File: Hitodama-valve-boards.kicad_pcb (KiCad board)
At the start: 2 copper layers, 74.9 x 73.7 mm, 25 parts, among them J1 Solenoid A, J2 Solenoid B, U1 LM358, U2 Pressure_b, U3 Pressure_a, U4 ChamberBoard_Holder, U5 Pololu-713

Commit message: remove useless texts
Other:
- board text removed: "If 1 layer Route only at the back!"
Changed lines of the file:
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@@
   (general
     (thickness 1.6)
-    (drawings 5)
+    (drawings 4)
     (tracks 281)
     (zones 0)
@@
       (effects (font (size 1 1) (thickness 0.15)))
     )
-    (fp_text value "Solenoid B" (at 2.78 7.75 180) (layer F.Fab)
+    (fp_text value "Solenoid B" (at -4.63 1.12 270) (layer F.Fab)
       (effects (font (size 1 1) (thickness 0.15)))
     )
@@
     (tags "mounting hole 3.2mm no annular m3")
     (attr virtual)
-    (fp_text reference H1 (at 0 -4.2) (layer F.SilkS)
+    (fp_text reference H1 (at 0 -4.2) (layer F.SilkS) hide
       (effects (font (size 1 1) (thickness 0.15)))
     )
@@
     (tags "mounting hole 3.2mm no annular m3")
     (attr virtual)
-    (fp_text reference H2 (at 0 4.2) (layer B.SilkS)
+    (fp_text reference H2 (at -0.5 5.25) (layer B.SilkS) hide
       (effects (font (size 1 1) (thickness 0.15)) (justify mirror))
     )
-    (fp_text value MountingHole (at 0 -4.2) (layer B.Fab)
+    (fp_text value MountingHole (at 0 -4.2) (layer B.Fab) hide
       (effects (font (size 1 1) (thickness 0.15)) (justify mirror))
     )
@@
       (effects (font (size 1 1) (thickness 0.15)) (justify mirror))
     )
-    (fp_text value MountingHole (at 0 6.54) (layer B.Fab)
+    (fp_text value MountingHole (at 0 6.54) (layer B.Fab) hide
       (effects (font (size 1 1) (thickness 0.15)) (justify mirror))
     )
@@
       (effects (font (size 1 1) (thickness 0.15)) (justify mirror))
     )
-    (fp_text value MountingHole (at 0 -4.2) (layer B.Fab)
+    (fp_text value MountingHole (at 0.1 -6.3441) (layer B.Fab) hide
       (effects (font (size 1 1) (thickness 0.15)) (justify mirror))
     )
@@
       (effects (font (size 1 1) (thickness 0.15)))
     )
-    (fp_text value "Solenoid A" (at 2.78 7.75 180) (layer F.Fab)
+    (fp_text value "Solenoid A" (at -4.75 1.07 270) (layer F.Fab)
       (effects (font (size 1 1) (thickness 0.15)))
     )
@@
     )
   )
-  (gr_text "If 1 layer Route only at the back!" (at 19 -4) (layer F.Cu)
-    (effects (font (size 1.5 1.5) (thickness 0.3)))
-  )
   (gr_line (start 74.93 73.66) (end 74.93 0) (layer Edge.Cuts) (width 0.15))

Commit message: generate seedstudio gerber files
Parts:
- added G***: LOGO, Hitodama_Logo:hitodama_n, F.Cu at (53.4, 67.2)

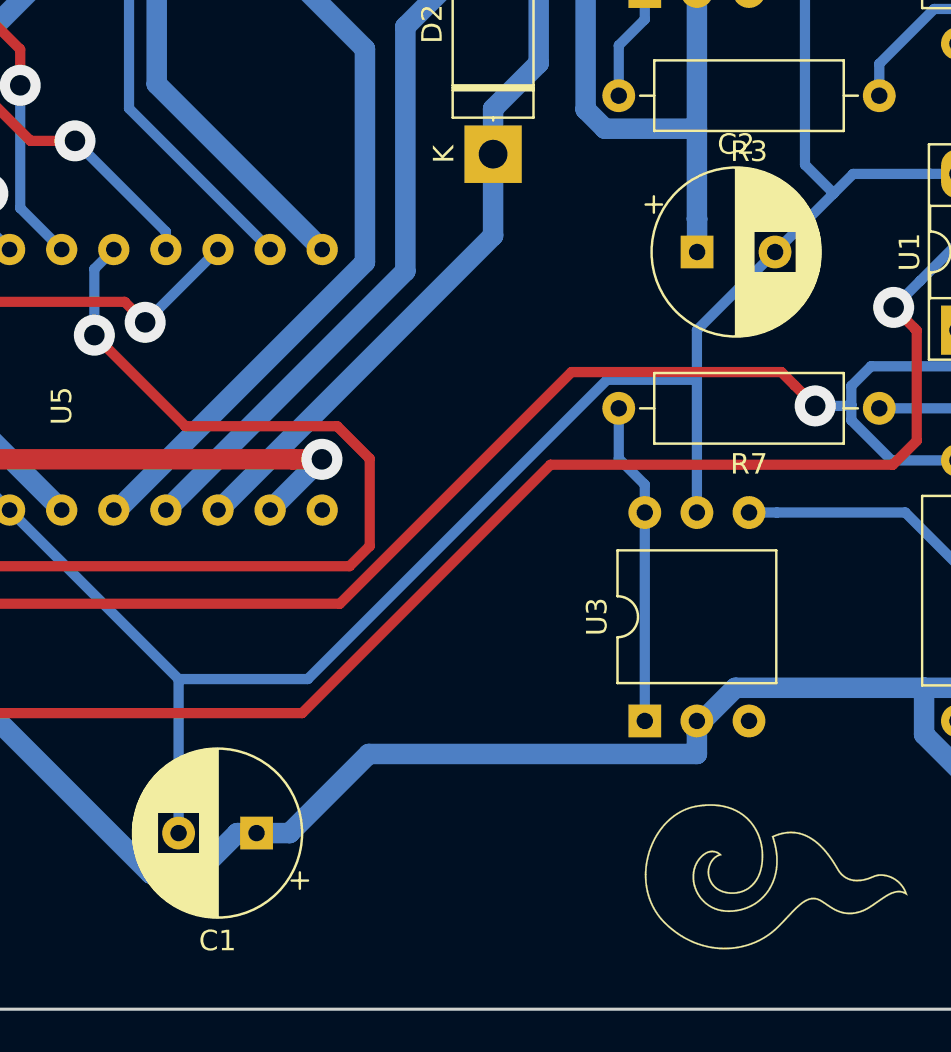
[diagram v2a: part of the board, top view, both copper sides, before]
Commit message: fix cap wrong orientation & teensy vcc.
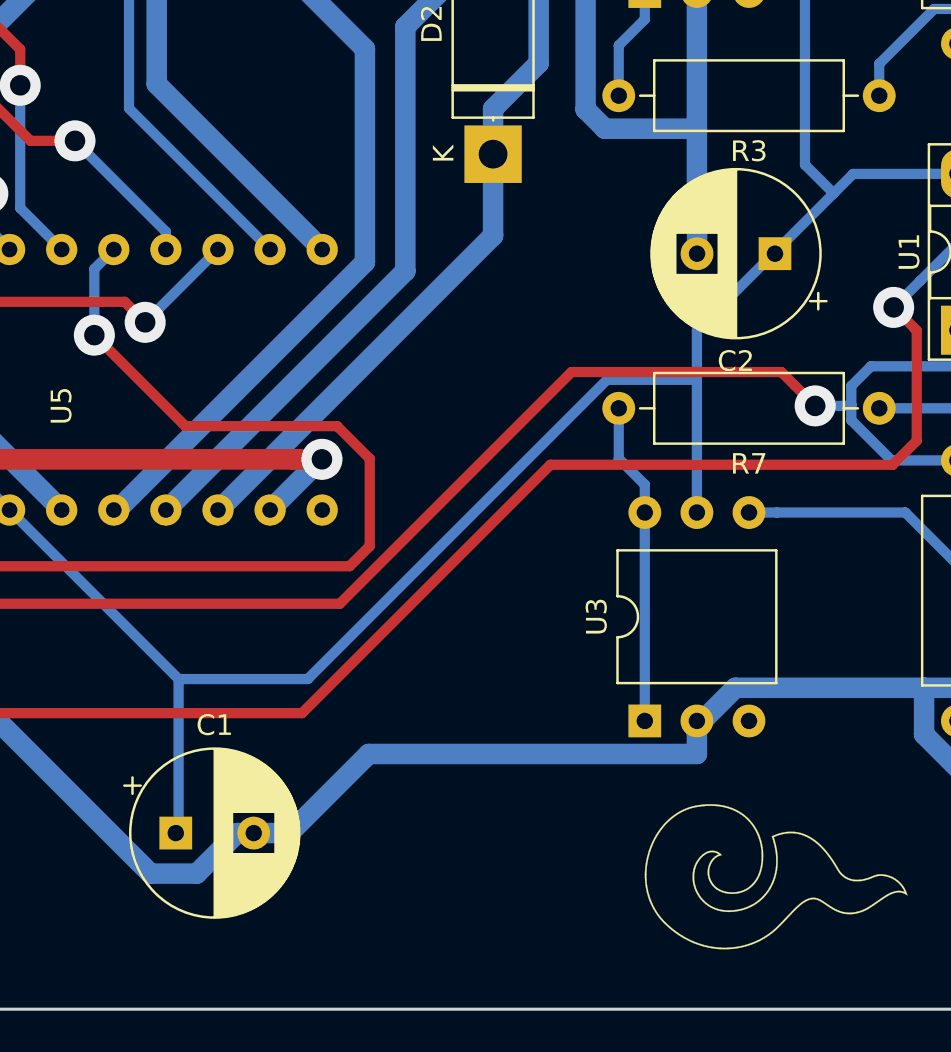
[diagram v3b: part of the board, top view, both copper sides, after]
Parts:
- moved C1 3.94 mm to (24.1, 65.1), turned to 0 degrees
- moved C2 3.80 mm to (53.3, 36.8), turned to 180 degrees
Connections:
- C1 pad 1: GND -> VCC
- C1 pad 2: VCC -> GND
- C2 pad 1: GND -> VCC
- C2 pad 2: VCC -> GND
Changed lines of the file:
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@@
   )
   (module Capacitor_THT:CP_Radial_D8.0mm_P3.80mm (layer F.Cu)
-    (at 28.067 65.0748 180)
+    (at 24.13 65.0748)
     (descr "CP, Radial series, Radial, pin pitch=3.80mm, , diameter=8mm, Electrolytic Capacitor")
     (tags "CP Radial series Radial pin pitch 3.80mm  diameter 8mm Electrolytic Capacitor")
-    (fp_text reference C1 (at 1.9 -5.25 180) (layer F.SilkS)
-      (effects (font (size 1 1) (thickness 0.15)))
-    )
-    (fp_text value "100uF 25v" (at 1.9 5.25 180) (layer F.Fab)
-      (effects (font (size 1 1) (thickness 0.15)))
-    )
-    (fp_text user %R (at 1.9 0 180) (layer F.Fab)
+    (fp_text reference C1 (at 1.9 -5.25) (layer F.SilkS)
+      (effects (font (size 1 1) (thickness 0.15)))
+    )
+    (fp_text value "100uF 25v" (at 1.9 5.25) (layer F.Fab)
+      (effects (font (size 1 1) (thickness 0.15)))
+    )
+    (fp_text user %R (at 1.9 0) (layer F.Fab)
       (effects (font (size 1 1) (thickness 0.15)))
     )
@@
     (fp_circle (center 1.9 0) (end 6.02 0) (layer F.SilkS) (width 0.12))
     (fp_circle (center 1.9 0) (end 5.9 0) (layer F.Fab) (width 0.1))
-    (pad 2 thru_hole circle (at 3.8 0 180) (size 1.6 1.6) (drill 0.8) (layers *.Cu *.Mask)
+    (pad 2 thru_hole circle (at 3.8 0) (size 1.6 1.6) (drill 0.8) (layers *.Cu *.Mask)
+      (net 2 GND))
+    (pad 1 thru_hole rect (at 0 0) (size 1.6 1.6) (drill 0.8) (layers *.Cu *.Mask)
       (net 1 VCC))
-    (pad 1 thru_hole rect (at 0 0 180) (size 1.6 1.6) (drill 0.8) (layers *.Cu *.Mask)
-      (net 2 GND))
     (model ${KISYS3DMOD}/Capacitor_THT.3dshapes/CP_Radial_D8.0mm_P3.80mm.wrl
       (at (xyz 0 0 0))
@@
   )
   (module Capacitor_THT:CP_Radial_D8.0mm_P3.80mm (layer F.Cu)
-    (at 49.5434 36.7481)
+    (at 53.34 36.83 180)
     (descr "CP, Radial series, Radial, pin pitch=3.80mm, , diameter=8mm, Electrolytic Capacitor")
     (tags "CP Radial series Radial pin pitch 3.80mm  diameter 8mm Electrolytic Capacitor")
-    (fp_text reference C2 (at 1.9 -5.25) (layer F.SilkS)
-      (effects (font (size 1 1) (thickness 0.15)))
-    )
-    (fp_text value "100uF 25v" (at 1.9 5.25) (layer F.Fab)
+    (fp_text reference C2 (at 1.9 -5.25 180) (layer F.SilkS)
+      (effects (font (size 1 1) (thickness 0.15)))
+    )
+    (fp_text value "100uF 25v" (at 1.9 5.25 180) (layer F.Fab)
       (effects (font (size 1 1) (thickness 0.15)))
     )
@@
     (fp_line (start -2.509698 -2.315) (end -1.709698 -2.315) (layer F.SilkS) (width 0.12))
     (fp_line (start -2.109698 -2.715) (end -2.109698 -1.915) (layer F.SilkS) (width 0.12))
-    (fp_text user %R (at 1.9 0 -270) (layer F.Fab)
-      (effects (font (size 1 1) (thickness 0.15)))
-    )
-    (pad 1 thru_hole rect (at 0 0) (size 1.6 1.6) (drill 0.8) (layers *.Cu *.Mask)
+    (fp_text user %R (at 1.9 0 -90) (layer F.Fab)
+      (effects (font (size 1 1) (thickness 0.15)))
+    )
+    (pad 1 thru_hole rect (at 0 0 180) (size 1.6 1.6) (drill 0.8) (layers *.Cu *.Mask)
+      (net 1 VCC))
+    (pad 2 thru_hole circle (at 3.8 0 180) (size 1.6 1.6) (drill 0.8) (layers *.Cu *.Mask)
       (net 2 GND))
-    (pad 2 thru_hole circle (at 3.8 0) (size 1.6 1.6) (drill 0.8) (layers *.Cu *.Mask)
-      (net 1 VCC))
     (model ${KISYS3DMOD}/Capacitor_THT.3dshapes/CP_Radial_D8.0mm_P3.80mm.wrl
       (at (xyz 0 0 0))

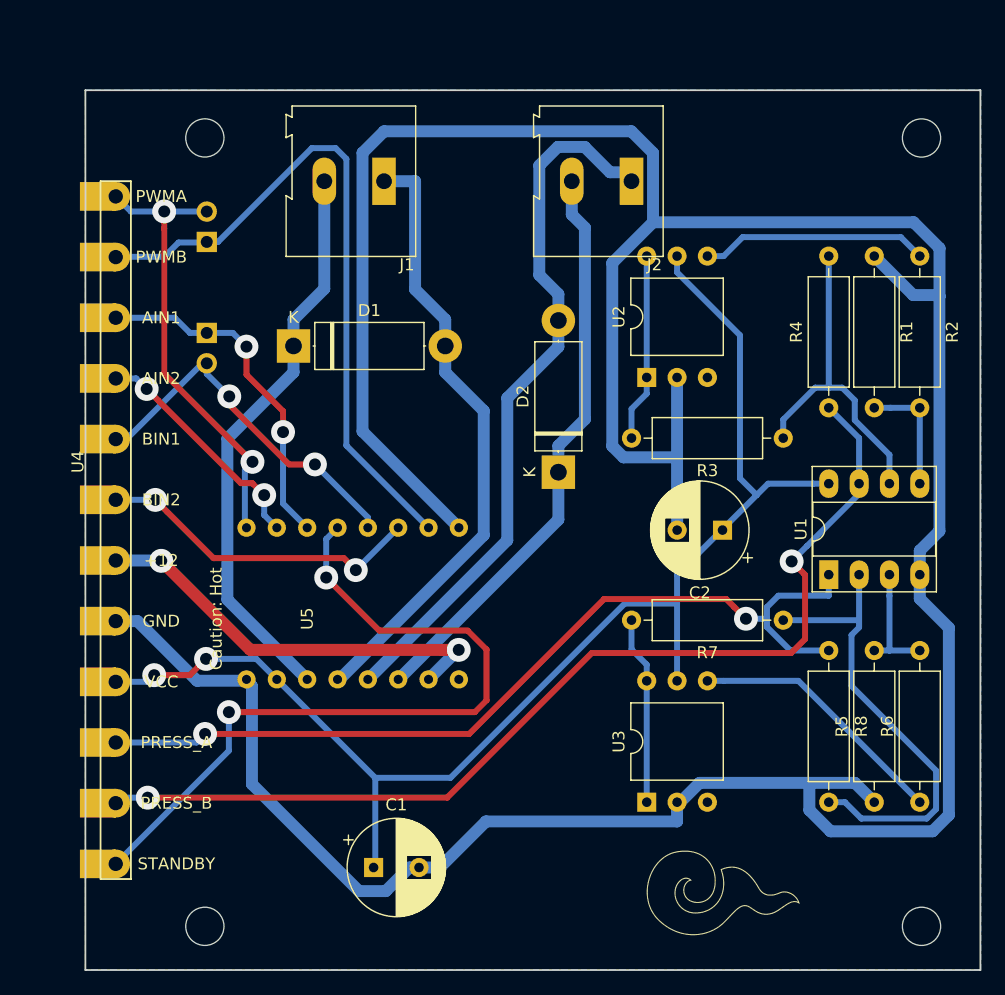
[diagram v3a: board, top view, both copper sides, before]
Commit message: change connectors into edge connector 5-5530843-3, TE Connectivity
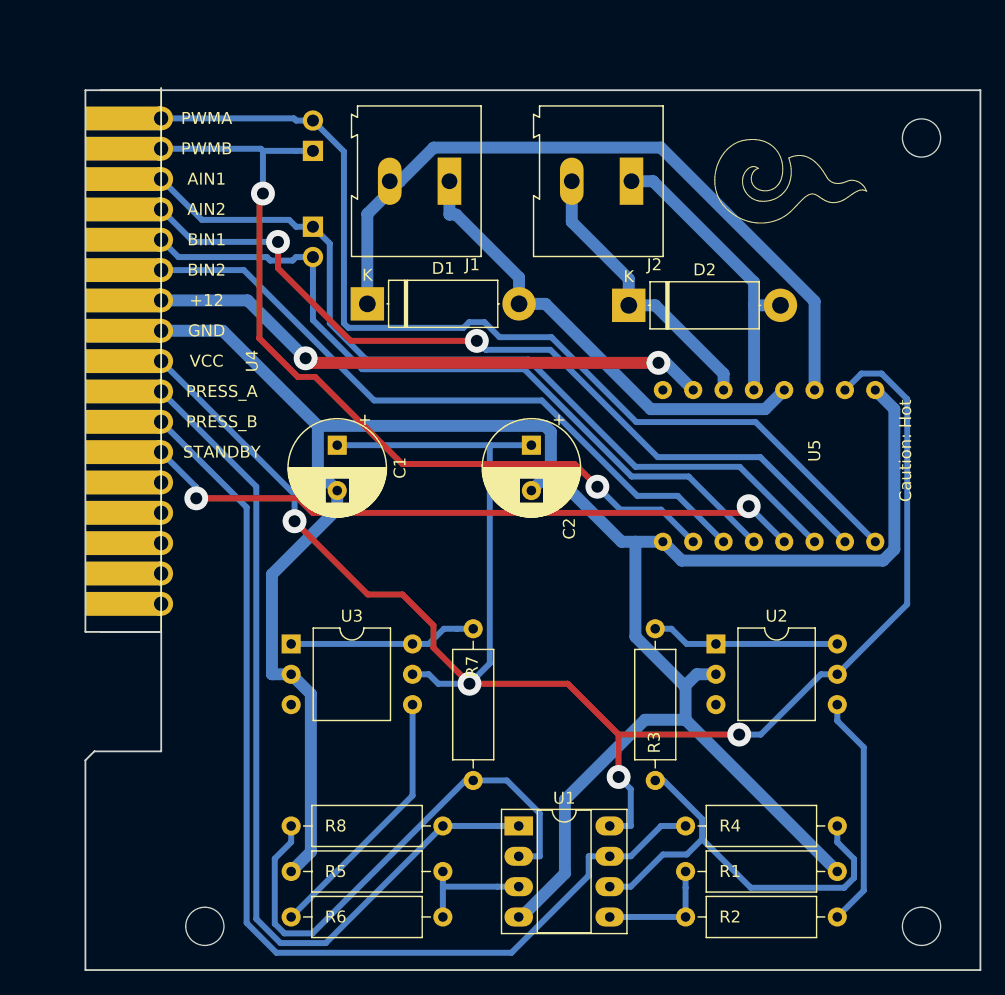
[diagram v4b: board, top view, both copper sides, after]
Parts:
- removed H4: MountingHole, MountingHole:MountingHole_3.2mm_M3
- U4: footprint chamber_board_holder:chamber_board_holder -> chamber_board_holder:chamber_board_holder_ 5-5530843-3_male
- moved G*** 59.8 mm to (59.1, 7.62)
- moved U5 57.9 mm to (66.1, 25.1), turned to 270 degrees
- moved R2 55.8 mm to (62.9, 69.2), turned to 180 degrees
- moved R6 53.5 mm to (17.2, 69.2), turned to 0 degrees
- moved R1 51.6 mm to (62.9, 65.4), turned to 180 degrees
- moved R5 49.2 mm to (17.2, 65.4), turned to 0 degrees
- moved R4 37.0 mm to (50.2, 61.6), turned to 0 degrees
- moved R8 35.5 mm to (29.9, 61.6), turned to 180 degrees
- moved C1 35.5 mm to (21.1, 29.7), turned to 270 degrees
- moved U1 33.4 mm to (36.3, 61.6), turned to 0 degrees
- moved U3 32.6 mm to (17.2, 46.4), turned to 0 degrees
- moved R3 30.6 mm to (47.7, 57.8), turned to 90 degrees
- moved R7 29.2 mm to (32.5, 57.8), turned to 90 degrees
- moved U2 23.1 mm to (52.8, 46.4), turned to 0 degrees
- moved C2 17.5 mm to (37.3, 29.7), turned to 270 degrees
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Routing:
- net GND: track 284.8 -> 193.2 mm
- net /A.IN.2: track 19.6 -> 70.1 mm
- net /A.PWM: track 38.0 -> 83.3 mm, vias 2 -> 0
- net VCC: track 113.0 -> 158.0 mm, vias 2 -> 4
- net /A.IN.1: track 29.2 -> 71.2 mm, vias 2 -> 0
- net /HVB-: track 59.9 -> 25.0 mm
- net /B.IN.1: track 30.9 -> 63.4 mm, vias 2 -> 0
- net /B.IN.2: track 27.6 -> 56.5 mm, vias 2 -> 0
- net /HVB+: track 48.7 -> 24.0 mm
- net /B.PWM: track 57.2 -> 72.0 mm, vias 0 -> 2
- net /HVA+: track 47.8 -> 60.9 mm
- net /HVA-: track 51.9 -> 39.5 mm
- net +12V: track 35.4 -> 47.7 mm
- net /stby: track 63.3 -> 56.3 mm
- net Net-(R3-Pad1): track 29.0 -> 36.0 mm
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- removed copper zone on B.Cu, net GND
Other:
- outline, holes or cut-outs redrawn

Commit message: added logos
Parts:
- moved G*** 2.62 mm to (59.7, 5.08)
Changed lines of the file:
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@@
-(kicad_pcb (version 20171130) (host pcbnew "(5.0.1)-4")
+(kicad_pcb (version 20171130) (host pcbnew 5.1.0)
   (general
     (thickness 1.6)
@@
     (zone_45_only no)
     (trace_min 0.2)
-    (segment_width 0.2)
-    (edge_width 0.15)
     (via_size 2)
     (via_drill 1)
@@
     (uvia_min_size 0.2)
     (uvia_min_drill 0.1)
+    (edge_width 0.15)
+    (segment_width 0.2)
     (pcb_text_width 0.3)
     (pcb_text_size 1.5 1.5)
@@
     (visible_elements 7FFFFFFF)
     (pcbplotparams
-      (layerselection 0x010fc_ffffffff)
-      (usegerberextensions false)
+      (layerselection 0x010f0_ffffffff)
+      (usegerberextensions true)
       (usegerberattributes false)
       (usegerberadvancedattributes false)
@@
       (outputformat 1)
       (mirror false)
-      (drillshape 1)
+      (drillshape 0)
       (scaleselection 1)
-      (outputdirectory ""))
+      (outputdirectory "SeedStudio-Avner/Valves/"))
   )
   (net 0 "")
@@
     (uvia_dia 0.3)
     (uvia_drill 0.1)
+    (diff_pair_width 0.3)
     (diff_pair_gap 0.3)
-    (diff_pair_width 0.3)
     (add_net /A.IN.1)
     (add_net /A.IN.2)
@@
     (uvia_dia 0.3)
     (uvia_drill 0.1)
+    (diff_pair_width 0.3)
     (diff_pair_gap 0.3)
-    (diff_pair_width 0.3)
     (add_net +12V)
     (add_net /HVA+)
@@
   )
   (module Hitodama_Logo:hitodama_n (layer F.Cu)
-    (at 59.055 7.62)
-    (fp_text reference G*** (at 0.025 -4.1) (layer F.SilkS) hide
+    (at 59.69 5.08)
+    (fp_text reference G*** (at 3.81 -7.62) (layer F.SilkS) hide
       (effects (font (size 1.524 1.524) (thickness 0.3)))
     )
-    (fp_text value LOGO (at 5.7 -4.25) (layer F.SilkS) hide
+    (fp_text value LOGO (at 8.89 -7.62) (layer F.SilkS) hide
       (effects (font (size 1.524 1.524) (thickness 0.3)))
     )
